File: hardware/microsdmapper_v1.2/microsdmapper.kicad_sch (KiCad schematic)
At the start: 26 parts, among them IC1 M29F010, IC2 HM628512, IC3 XC95144XL_TQ100, J1 Conn_02x03_Odd_Even, J2 Micro_SD_Card_Det1, U1 ESP8266-12E/ESP-12E, U2 LM1117MP-3.3, X1 25 Mhz

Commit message: v1.2 and images
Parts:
- added D1: LED, LED_THT:LED_D3.0mm, symbol Device:LED
- added Q1: BC858, Package_TO_SOT_SMD:SOT-23, symbol Transistor_BJT:BC858
- added R10: 330, Resistor_SMD:R_0603_1608Metric_Pad0.98x0.95mm_HandSolder, symbol Device:R
- added R9: 4.7K, Resistor_SMD:R_0603_1608Metric_Pad0.98x0.95mm_HandSolder, symbol Device:R
- J1: footprint Connector_PinHeader_2.54mm:PinHeader_1x05_P2.54mm_Vertical -> Connector_PinHeader_2.54mm:PinHeader_2x03_P2.54mm_Vertical
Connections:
- net +5V: now also Q1.2 (E)
- net GND: now also R10.1
- net SD_CS0: now also R9.1
- new net: Q1.1 (B), R9.2
- new net: D1.2 (A), Q1.3 (C)
- new net: D1.1 (K), R10.2
- no-connect marks 55 -> 56
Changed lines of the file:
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@@
   (title_block
     (title "microSDMapper v1.2")
-    (date "2023-05-28")
+    (date "2023-06-06")
     (rev "1.2")
     (company "The Retro Hacker")
@@
   (no_connect (at 154.94 223.52))
   (no_connect (at 356.87 40.64))
+  (no_connect (at 166.37 271.78))
   (no_connect (at 356.87 43.18))
   (no_connect (at 302.26 171.45))
@@
     (stroke (width 0) (type default))
   )
+  (wire (pts (xy 195.58 271.78) (xy 179.07 271.78))
+    (stroke (width 0) (type default))
+  )
   (wire (pts (xy 110.49 53.34) (xy 115.57 53.34))
     (stroke (width 0) (type default))
@@
     (stroke (width 0) (type default))
   )
+  (wire (pts (xy 368.3 219.71) (xy 372.11 219.71))
+    (stroke (width 0) (type default))
+  )
   (wire (pts (xy 317.5 35.56) (xy 336.55 35.56))
     (stroke (width 0) (type default))
@@
     (stroke (width 0) (type default))
   )
-  (wire (pts (xy 195.58 271.78) (xy 179.07 271.78))
-    (stroke (width 0) (type default))
-  )
   (wire (pts (xy 72.39 132.08) (xy 81.28 132.08))
     (stroke (width 0) (type default))
@@
     (stroke (width 0) (type default))
   )
+  (wire (pts (xy 373.38 233.68) (xy 379.73 233.68))
+    (stroke (width 0) (type default))
+  )
   (wire (pts (xy 292.1 64.77) (xy 292.1 54.61))
     (stroke (width 0) (type default))
@@
     (stroke (width 0) (type default))
   )
+  (wire (pts (xy 360.68 233.68) (xy 365.76 233.68))
+    (stroke (width 0) (type default))
+  )
   (wire (pts (xy 132.08 241.3) (xy 132.08 214.63))
     (stroke (width 0) (type default))
@@
     (stroke (width 0) (type default))
   )
+  (wire (pts (xy 379.73 219.71) (xy 384.81 219.71))
+    (stroke (width 0) (type default))
+  )
   (wire (pts (xy 292.1 220.98) (xy 266.7 220.98))
     (stroke (width 0) (type default))
   )
+  (wire (pts (xy 360.68 209.55) (xy 360.68 214.63))
+    (stroke (width 0) (type default))
+  )
+  (wire (pts (xy 387.35 233.68) (xy 392.43 233.68))
+    (stroke (width 0) (type default))
+  )
   (wire (pts (xy 54.61 87.63) (xy 59.69 87.63))
     (stroke (width 0) (type default))
@@
   )
   (wire (pts (xy 39.37 207.01) (xy 48.26 207.01))
+    (stroke (width 0) (type default))
+  )
+  (wire (pts (xy 360.68 224.79) (xy 360.68 233.68))
     (stroke (width 0) (type default))
   )
@@
   (label "MSX_A7" (at 325.12 180.34 270) (fields_autoplaced)
     (effects (font (size 1.27 1.27)) (justify right bottom))
+  )
+  (label "SD_CS0" (at 384.81 219.71 0) (fields_autoplaced)
+    (effects (font (size 1.2446 1.2446)) (justify left bottom))
   )
   (label "ROM_CS" (at 363.22 140.97 0) (fields_autoplaced)
@@
     )
   )
+  (symbol (lib_id "power:+5V") (at 360.68 209.55 0) (unit 1)
+    (in_bom yes) (on_board yes) (dnp no) (fields_autoplaced)
+    (property "Reference" "#PWR020" (at 360.68 213.36 0)
+      (effects (font (size 1.27 1.27)) hide)
+    )
+    (property "Value" "+5V" (at 360.68 205.74 0)
+      (effects (font (size 1.27 1.27)))
+    )
+    (property "Footprint" "" (at 360.68 209.55 0)
+      (effects (font (size 1.27 1.27)) hide)
+    )
+    (property "Datasheet" "" (at 360.68 209.55 0)
+      (effects (font (size 1.27 1.27)) hide)
+    )
+    (pin "1")
+    (instances
+      (project "microsdmapper"
+        (path "/c945c20f-3691-483a-95d3-09d0b04a2d96"
+          (reference "#PWR020") (unit 1)
+        )
+      )
+    )
+  )
   (symbol (lib_id "Connector_Generic:Conn_02x03_Odd_Even") (at 171.45 269.24 0) (unit 1)
     (in_bom yes) (on_board yes) (dnp no) (fields_autoplaced)
@@
       (effects (font (size 1.27 1.27)))
     )
-    (property "Footprint" "Connector_PinHeader_2.54mm:PinHeader_1x05_P2.54mm_Vertical" (at 171.45 269.24 0)
+    (property "Footprint" "Connector_PinHeader_2.54mm:PinHeader_2x03_P2.54mm_Vertical" (at 171.45 269.24 0)
       (effects (font (size 1.27 1.27)) hide)
     )
@@
     )
   )
+  (symbol (lib_id "Device:R") (at 375.92 219.71 270) (unit 1)
+    (in_bom yes) (on_board yes) (dnp no) (fields_autoplaced)
+    (property "Reference" "R9" (at 375.92 214.63 90)
+      (effects (font (size 1.27 1.27)))
+    )
+    (property "Value" "4.7K" (at 375.92 217.17 90)
+      (effects (font (size 1.27 1.27)))
+    )
+    (property "Footprint" "Resistor_SMD:R_0603_1608Metric_Pad0.98x0.95mm_HandSolder" (at 375.92 217.932 90)
+      (effects (font (size 1.27 1.27)) hide)
+    )
+    (property "Datasheet" "~" (at 375.92 219.71 0)
+      (effects (font (size 1.27 1.27)) hide)
+    )
+    (pin "1")
+    (pin "2")
+    (instances
+      (project "microsdmapper"
+        (path "/c945c20f-3691-483a-95d3-09d0b04a2d96"
+          (reference "R9") (unit 1)
+        )
+      )
+    )
+  )
   (symbol (lib_id "power:GND") (at 191.77 123.19 0) (unit 1)
     (in_bom yes) (on_board yes) (dnp no) (fields_autoplaced)
@@
         (path "/c945c20f-3691-483a-95d3-09d0b04a2d96"
           (reference "R1") (unit 1)
+        )
+      )
+    )
+  )
+  (symbol (lib_id "Transistor_BJT:BC858") (at 363.22 219.71 180) (unit 1)
+    (in_bom yes) (on_board yes) (dnp no) (fields_autoplaced)
+    (property "Reference" "Q1" (at 358.14 219.075 0)
+      (effects (font (size 1.27 1.27)) (justify left))
+    )
+    (property "Value" "BC858" (at 358.14 221.615 0)
+      (effects (font (size 1.27 1.27)) (justify left))
+    )
+    (property "Footprint" "Package_TO_SOT_SMD:SOT-23" (at 358.14 217.805 0)
+      (effects (font (size 1.27 1.27) italic) (justify left) hide)
+    )
+    (property "Datasheet" "https://www.onsemi.com/pub/Collateral/BC860-D.pdf" (at 363.22 219.71 0)
+      (effects (font (size 1.27 1.27)) (justify left) hide)
+    )
+    (pin "1")
+    (pin "2")
+    (pin "3")
+    (instances
+      (project "microsdmapper"
+        (path "/c945c20f-3691-483a-95d3-09d0b04a2d96"
+          (reference "Q1") (unit 1)
         )
       )
@@
     )
   )
+  (symbol (lib_id "Device:LED") (at 369.57 233.68 180) (unit 1)
+    (in_bom yes) (on_board yes) (dnp no) (fields_autoplaced)
+    (property "Reference" "D1" (at 371.1575 227.33 0)
+      (effects (font (size 1.27 1.27)))
+    )
+    (property "Value" "LED" (at 371.1575 229.87 0)
+      (effects (font (size 1.27 1.27)))
+    )
+    (property "Footprint" "LED_THT:LED_D3.0mm" (at 369.57 233.68 0)
+      (effects (font (size 1.27 1.27)) hide)
+    )
+    (property "Datasheet" "~" (at 369.57 233.68 0)
+      (effects (font (size 1.27 1.27)) hide)
+    )
+    (pin "1")
+    (pin "2")
+    (instances
+      (project "microsdmapper"
+        (path "/c945c20f-3691-483a-95d3-09d0b04a2d96"
+          (reference "D1") (unit 1)
+        )
+      )
+    )
+  )
+  (symbol (lib_id "Device:R") (at 383.54 233.68 270) (unit 1)
+    (in_bom yes) (on_board yes) (dnp no) (fields_autoplaced)
+    (property "Reference" "R10" (at 383.54 228.6 90)
+      (effects (font (size 1.27 1.27)))
+    )
+    (property "Value" "330" (at 383.54 231.14 90)
+      (effects (font (size 1.27 1.27)))
+    )
+    (property "Footprint" "Resistor_SMD:R_0603_1608Metric_Pad0.98x0.95mm_HandSolder" (at 383.54 231.902 90)
+      (effects (font (size 1.27 1.27)) hide)
+    )
+    (property "Datasheet" "~" (at 383.54 233.68 0)
+      (effects (font (size 1.27 1.27)) hide)
+    )
+    (pin "1")
+    (pin "2")
+    (instances
+      (project "microsdmapper"
+        (path "/c945c20f-3691-483a-95d3-09d0b04a2d96"
+          (reference "R10") (unit 1)
+        )
+      )
+    )
+  )
   (symbol (lib_id "power:GND") (at 54.61 107.95 0) (unit 1)
     (in_bom yes) (on_board yes) (dnp no) (fields_autoplaced)
@@
         )
       )
+    )
+  )
+  (symbol (lib_id "power:GND") (at 392.43 233.68 90) (unit 1)
+    (in_bom yes) (on_board yes) (dnp no) (fields_autoplaced)
+    (property "Reference" "#PWR021" (at 398.78 233.68 0)
+      (effects (font (size 1.27 1.27)) hide)
+    )
+    (property "Value" "GND" (at 396.24 234.315 90)
+      (effects (font (size 1.27 1.27)) (justify right))
+    )
+    (property "Footprint" "" (at 392.43 233.68 0)
+      (effects (font (size 1.27 1.27)) hide)
+    )
+    (property "Datasheet" "" (at 392.43 233.68 0)
+      (effects (font (size 1.27 1.27)) hide)
+    )
+    (pin "1")
+    (instances
+      (project "microsdmapper"
+        (path "/c945c20f-3691-483a-95d3-09d0b04a2d96"
+          (reference "#PWR021") (unit 1)
+        )
+      )

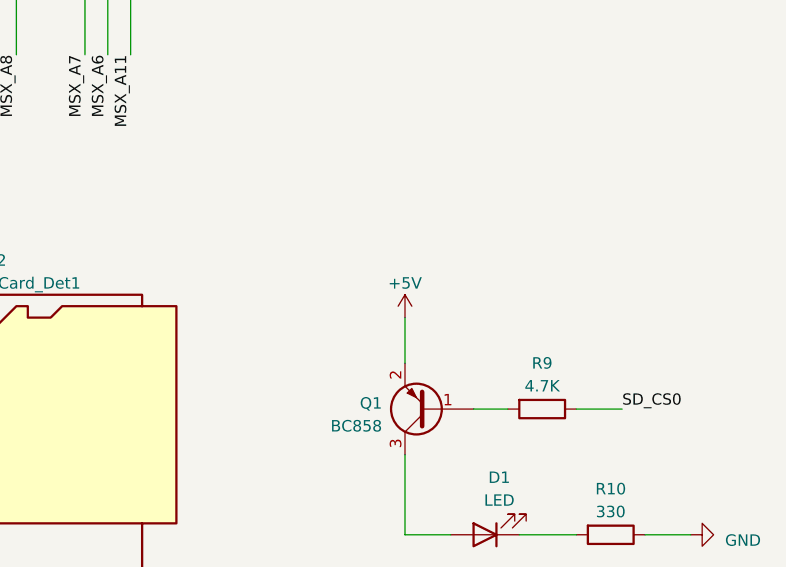
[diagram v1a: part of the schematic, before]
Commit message: Fix led and new gerbers
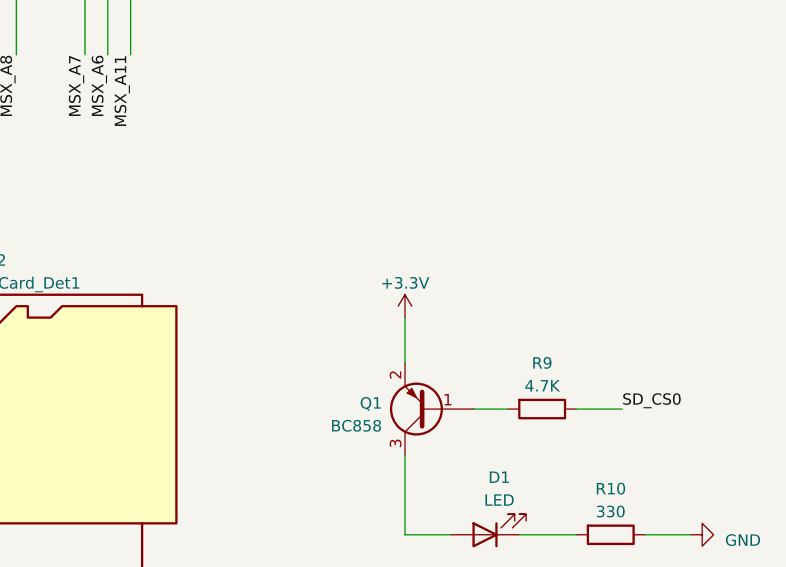
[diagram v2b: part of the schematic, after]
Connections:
- net +3.3V: now also Q1.2 (E)
- net +5V: no longer Q1.2 (E)
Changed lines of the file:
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@@
-    )
-  )
-  (symbol (lib_id "power:+5V") (at 360.68 209.55 0) (unit 1)
-    (in_bom yes) (on_board yes) (dnp no) (fields_autoplaced)
-    (property "Reference" "#PWR020" (at 360.68 213.36 0)
-      (effects (font (size 1.27 1.27)) hide)
-    )
-    (property "Value" "+5V" (at 360.68 205.74 0)
-      (effects (font (size 1.27 1.27)))
-    )
-    (property "Footprint" "" (at 360.68 209.55 0)
-      (effects (font (size 1.27 1.27)) hide)
-    )
-    (property "Datasheet" "" (at 360.68 209.55 0)
-      (effects (font (size 1.27 1.27)) hide)
-    )
-    (pin "1")
-    (instances
-      (project "microsdmapper"
-        (path "/c945c20f-3691-483a-95d3-09d0b04a2d96"
-          (reference "#PWR020") (unit 1)
-        )
-      )
     )
   )
@@
         )
       )
+    )
+  )
+  (symbol (lib_id "power:+3.3V") (at 360.68 209.55 0) (unit 1)
+    (in_bom yes) (on_board yes) (dnp no) (fields_autoplaced)
+    (property "Reference" "#PWR020" (at 360.68 213.36 0)
+      (effects (font (size 1.27 1.27)) hide)
+    )
+    (property "Value" "+3.3V" (at 360.68 205.74 0)
+      (effects (font (size 1.27 1.27)))
+    )
+    (property "Footprint" "" (at 360.68 209.55 0)
+      (effects (font (size 1.27 1.27)) hide)
+    )
+    (property "Datasheet" "" (at 360.68 209.55 0)
+      (effects (font (size 1.27 1.27)) hide)
+    )
+    (pin "1")
+    (instances
+      (project "microsdmapper"
+        (path "/c945c20f-3691-483a-95d3-09d0b04a2d96"
+          (reference "#PWR020") (unit 1)
+        )
+      )
